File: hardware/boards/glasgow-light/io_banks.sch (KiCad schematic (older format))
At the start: 20 parts, among them J10 AUX, J4 Conn_01x02, U5 ICE40UP5K-SG48ITR

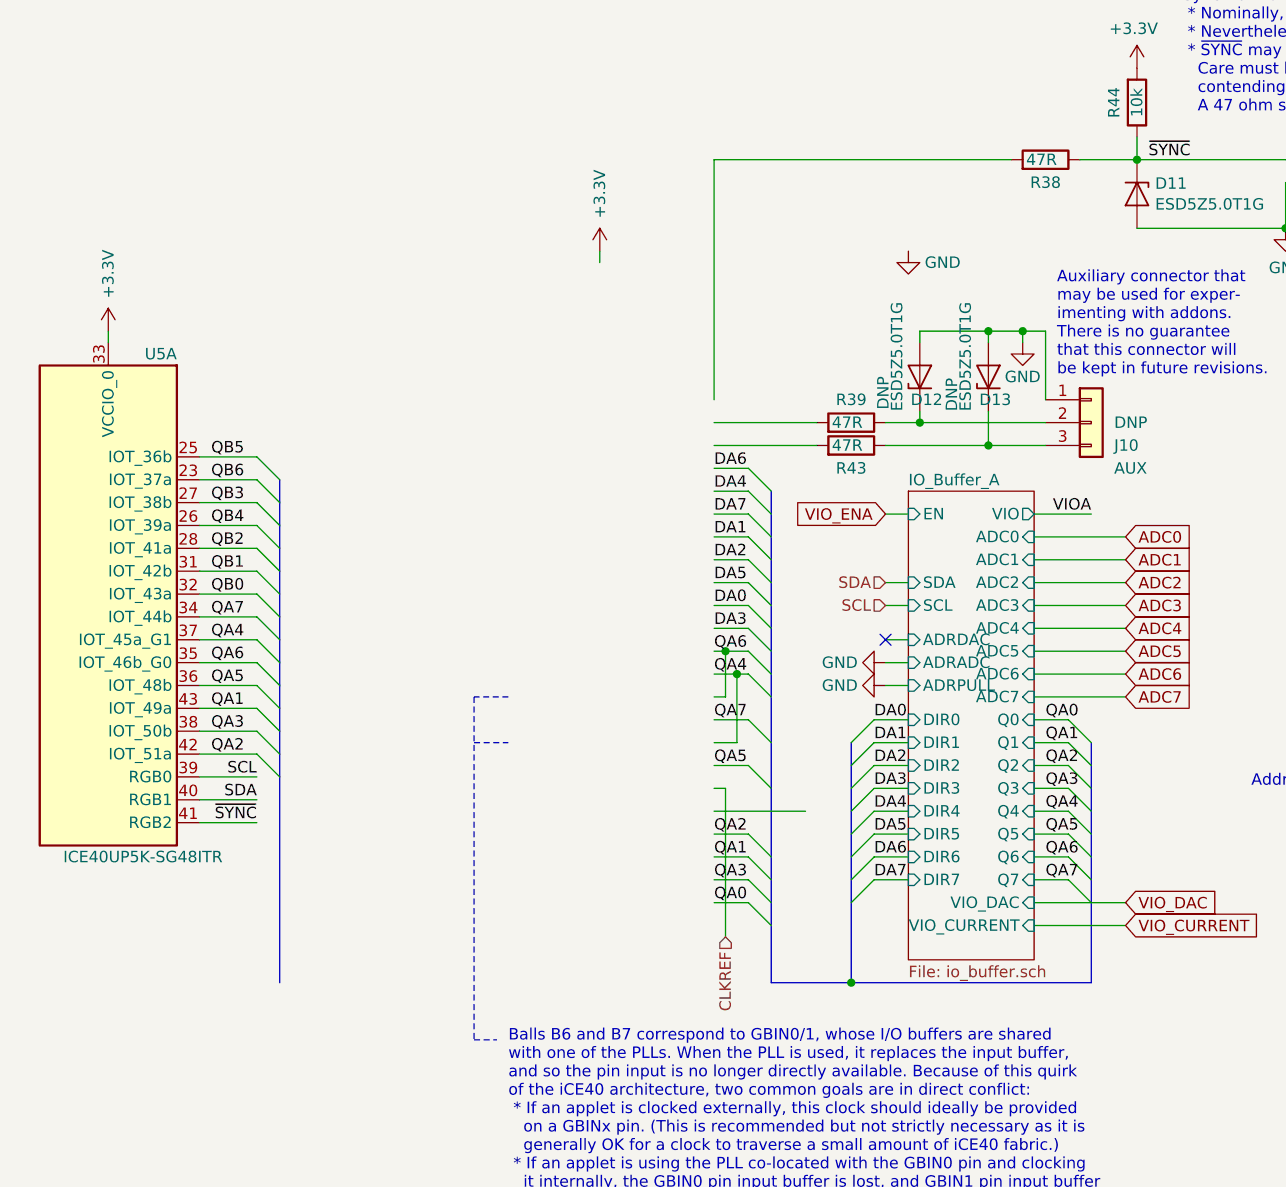
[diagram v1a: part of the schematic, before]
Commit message: start routing FPGA
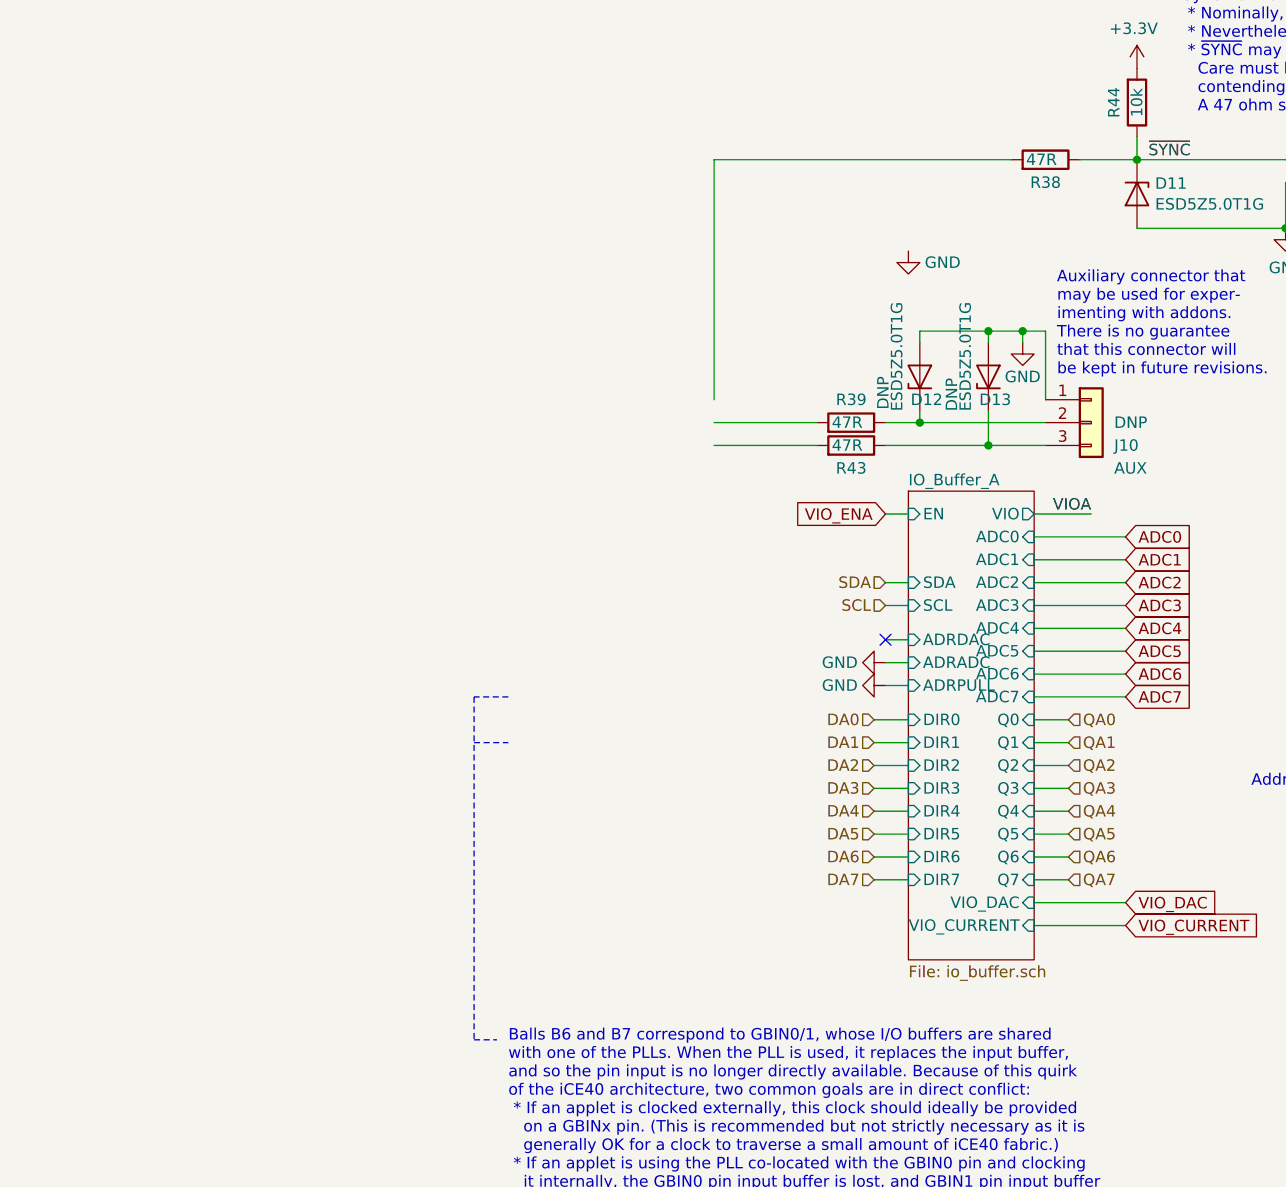
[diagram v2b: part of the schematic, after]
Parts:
- removed U5: ICE40UP5K-SG48ITR, Package_DFN_QFN:QFN-48-1EP_7x7mm_P0.5mm_EP5.15x5.15mm, symbol FPGA_Lattice:ICE40UP5K-SG48ITR
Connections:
- net labels removed: CLKREF, QB0, QB1, QB2, QB3, QB4, QB5, QB6
- wire segments 119 -> 75

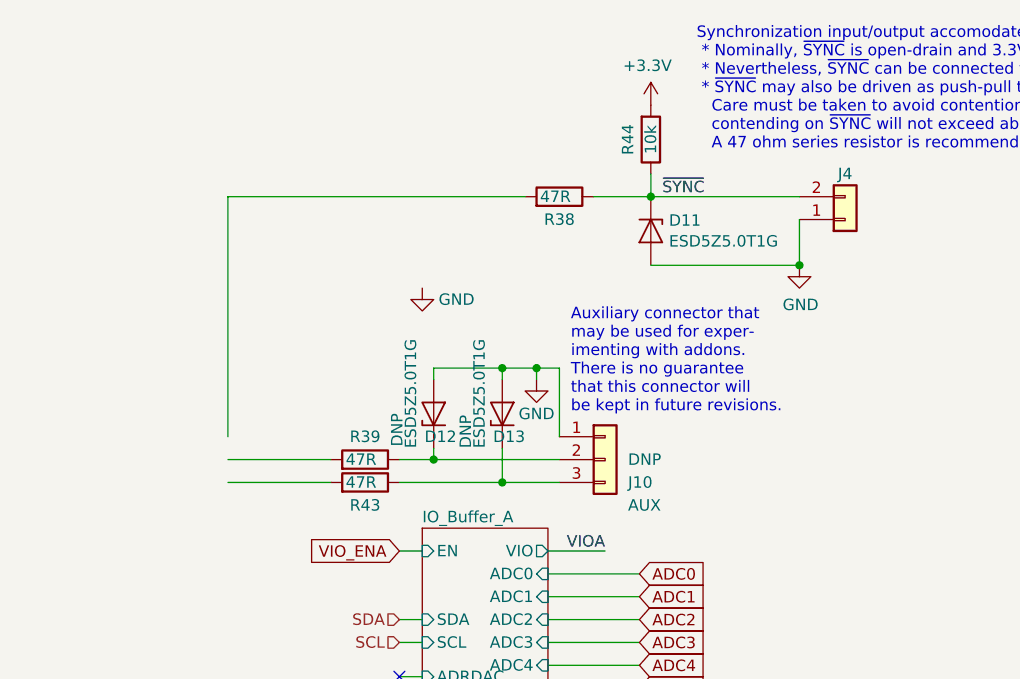
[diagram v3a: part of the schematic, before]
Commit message: replace SYNC and AUX connectors by test points
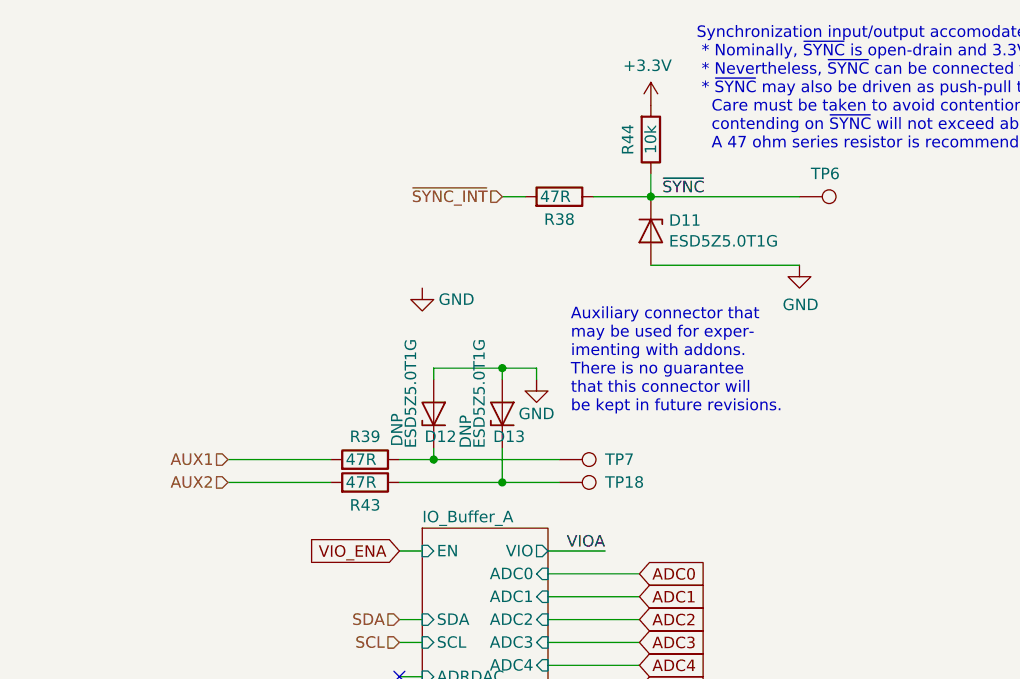
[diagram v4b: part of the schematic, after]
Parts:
- removed J10: AUX, Connector_PinHeader_2.54mm:PinHeader_1x03_P2.54mm_Vertical, symbol Connector_Generic:Conn_01x03
- removed J4: Conn_01x02, Glasgow:Molex_KK-254_1x02_P2.54mm_Horizontal, symbol Connector_Generic:Conn_01x02
- added TP18, TP6, TP7: SYNC, TestPoint:TestPoint_Pad_D1.0mm, symbol Connector:TestPoint
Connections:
- net labels added: AUX1, AUX2, ~SYNC_INT
- wire segments 75 -> 71
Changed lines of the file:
@@
 	2650 4250 2550 4250
-$Comp
-L Connector_Generic:Conn_01x03 J10
-U 1 1 5C072C23
-P 3450 3550
-F 0 "J10" H 3550 3450 50  0000 L CNN
-F 1 "AUX" H 3550 3350 50  0000 L CNN
-F 2 "Connector_PinHeader_2.54mm:PinHeader_1x03_P2.54mm_Vertical" H 3450 3550 50  0001 C CNN
-F 3 "~" H 3450 3550 50  0001 C CNN
-F 4 "conn-th-01in-3-1-hdr" H 3450 3550 50  0001 C CNN "1b2-bom-key"
-F 5 "DNP" H 3550 3550 50  0000 L CNN "DNP"
-	1    3450 3550
-	1    0    0    -1
-$EndComp
 $Comp
 L power:GND #PWR?
@@
 $EndComp
 $Comp
-L Connector_Generic:Conn_01x02 J?
-U 1 1 5C961091
-P 4500 2500
-AR Path="/5C961091" Ref="J?"  Part="1"
-AR Path="/5C7B59B0/5C961091" Ref="J4"  Part="1"
-F 0 "J4" H 4500 2300 50  0000 C CNN
-F 1 "Conn_01x02" H 4580 2401 50  0001 L CNN
-F 2 "Glasgow:Molex_KK-254_1x02_P2.54mm_Horizontal" H 4500 2500 50  0001 C CNN
-F 3 "https://www.mouser.hk/datasheet/2/418/NG_CD_640455_Y3-1255934.pdf" H 4500 2500 50  0001 C CNN
-F 4 "Molex" H -6100 -350 50  0001 C CNN "Mfg"
-F 5 "22-05-3021" H -6100 -350 50  0001 C CNN "MPN"
-F 6 "conn-th-01in-2-1-hdr-ra" H 4500 2500 50  0001 C CNN "1b2-bom-key"
-	1    4500 2500
-	1    0    0    1
-$EndComp
-$Comp
 L power:GND #PWR?
 U 1 1 5C961098
@@
 	1    0    0    -1
 $EndComp
-Wire Wire Line
-	1800 2400 1800 3450
 $Comp
 L Device:R R?
@@
 Connection ~ 3650 2400
 Wire Wire Line
-	4300 2500 4300 2700
-Connection ~ 4300 2700
-Wire Wire Line
 	3650 2400 4300 2400
 Wire Wire Line
@@
 $EndComp
 Wire Wire Line
-	3250 3150 3150 3150
-Wire Wire Line
 	3150 3150 3150 3200
 Wire Wire Line
-	3250 3150 3250 3450
-Wire Wire Line
 	3150 3150 3000 3150
 Wire Wire Line
 	3000 3150 3000 3200
-Connection ~ 3150 3150
 Wire Wire Line
 	3000 3150 2700 3150
@@
 $EndComp
 Wire Wire Line
-	1800 2400 3100 2400
+	3000 2400 3100 2400
 Wire Wire Line
 	2550 4700 2650 4700
@@
 Wire Wire Line
 	2650 5550 2500 5550
+Text HLabel 3000 2400 0    50   Input ~ 0
+~SYNC_INT
+$Comp
+L Connector:TestPoint TP?
+U 1 1 612A8BE6
+P 4300 2400
+AR Path="/612A8BE6" Ref="TP?"  Part="1"
+AR Path="/5C7B59B0/612A8BE6" Ref="TP6"  Part="1"
+F 0 "TP6" V 4200 2450 50  0000 L CNN
+F 1 "SYNC" V 4404 2474 50  0001 C CNN
+F 2 "TestPoint:TestPoint_Pad_D1.0mm" H 4500 2400 50  0001 C CNN
+F 3 "~" H 4500 2400 50  0001 C CNN
+	1    4300 2400
+	0    1    1    0
+$EndComp
+$Comp
+L Connector:TestPoint TP?
+U 1 1 6134742E
+P 3250 3550
+AR Path="/6134742E" Ref="TP?"  Part="1"
+AR Path="/5C7B59B0/6134742E" Ref="TP7"  Part="1"
+F 0 "TP7" V 3250 3750 50  0000 L CNN
+F 1 "SYNC" V 3354 3624 50  0001 C CNN
+F 2 "TestPoint:TestPoint_Pad_D1.0mm" H 3450 3550 50  0001 C CNN
+F 3 "~" H 3450 3550 50  0001 C CNN
+	1    3250 3550
+	0    1    1    0
+$EndComp
+$Comp
+L Connector:TestPoint TP?
+U 1 1 6134792A
+P 3250 3650
+AR Path="/6134792A" Ref="TP?"  Part="1"
+AR Path="/5C7B59B0/6134792A" Ref="TP18"  Part="1"
+F 0 "TP18" V 3250 3850 50  0000 L CNN
+F 1 "SYNC" V 3354 3724 50  0001 C CNN
+F 2 "TestPoint:TestPoint_Pad_D1.0mm" H 3450 3650 50  0001 C CNN
+F 3 "~" H 3450 3650 50  0001 C CNN
+	1    3250 3650
+	0    1    1    0
+$EndComp
+Text HLabel 1800 3550 0    50   Input ~ 0
+AUX1
+Text HLabel 1800 3650 0    50   Input ~ 0
+AUX2
 $EndSCHEMATC

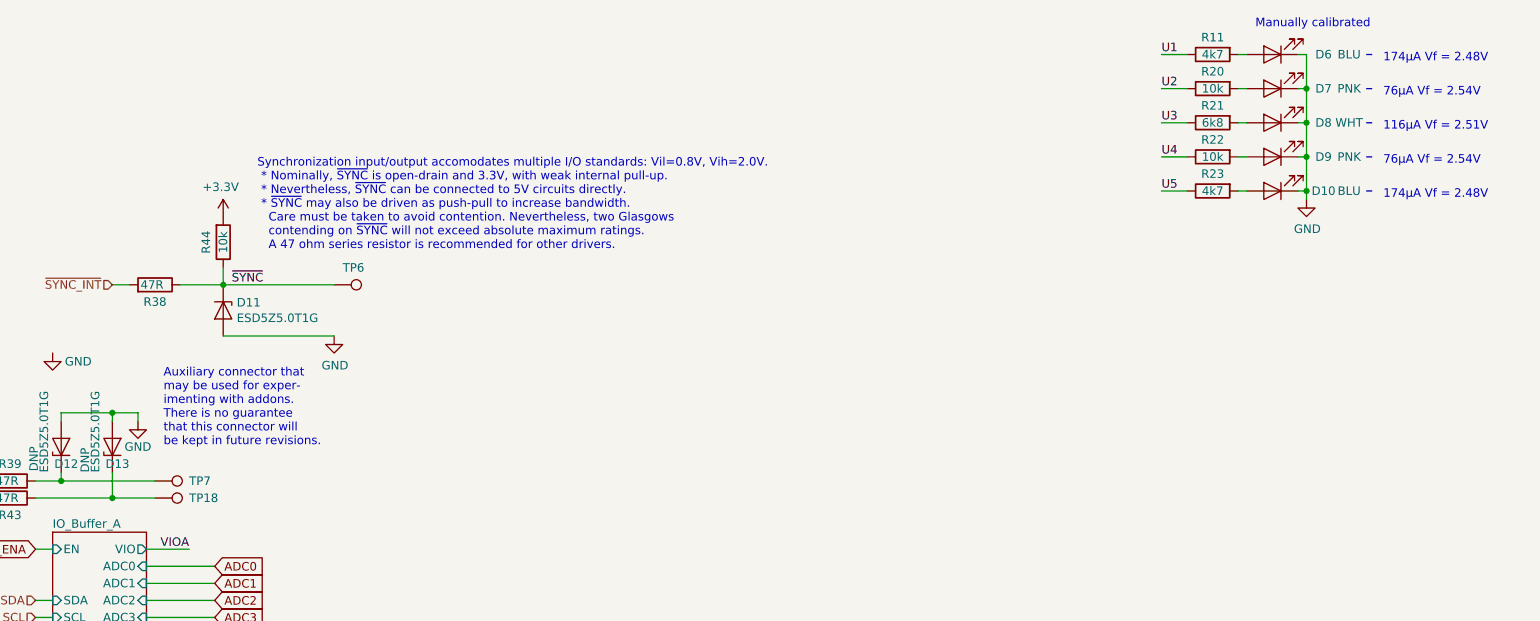
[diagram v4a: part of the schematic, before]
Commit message: most components are placed
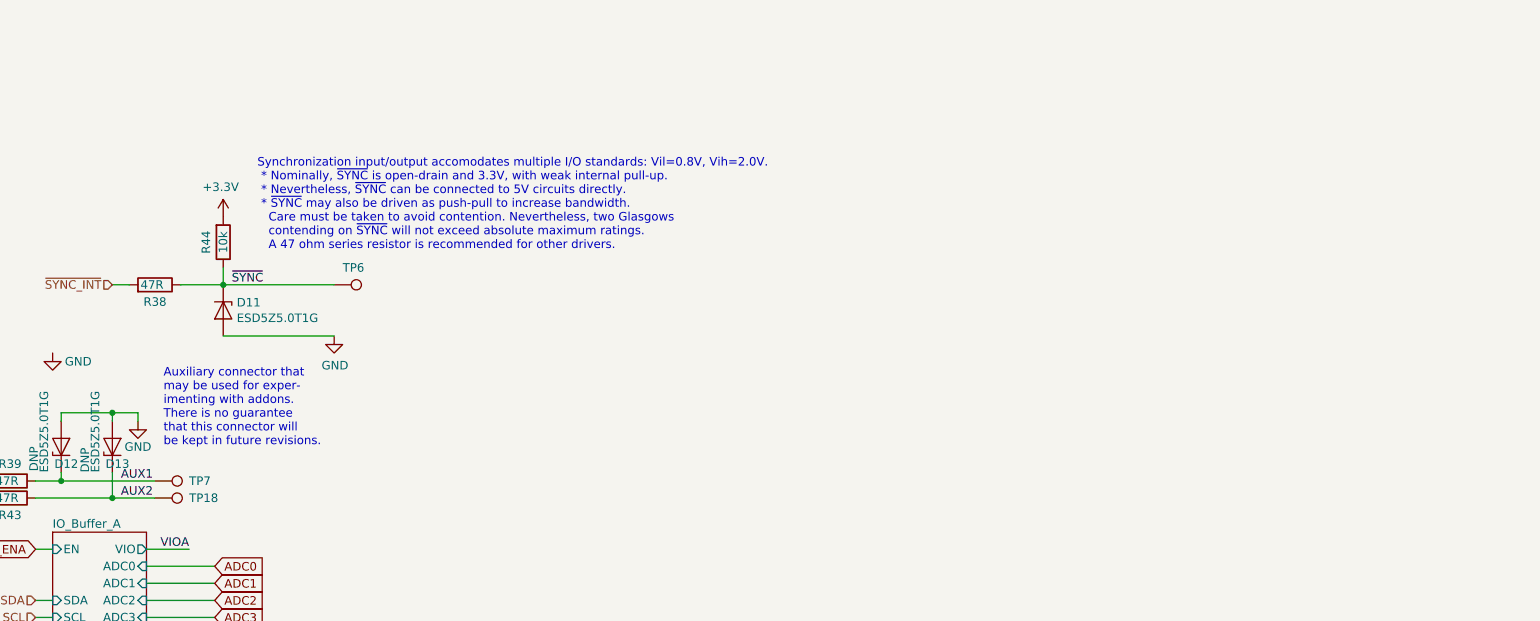
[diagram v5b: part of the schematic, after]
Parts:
- removed D10, D6: BLU, LED_SMD:LED_0603_1608Metric, symbol Device:LED
- removed D7, D9: PNK, LED_SMD:LED_0603_1608Metric, symbol Device:LED
- removed D8: WHT, LED_SMD:LED_0603_1608Metric, symbol Device:LED
- removed R11, R23: 4k7, Resistor_SMD:R_0402_1005Metric, symbol Device:R
- removed R20, R22: 10k, Resistor_SMD:R_0402_1005Metric, symbol Device:R
- removed R21: 6k8, Resistor_SMD:R_0402_1005Metric, symbol Device:R
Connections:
- net AUX1~: now reaches D12.1 (K), R39.1, TP7.1
- net AUX2~: now reaches D13.1 (K), R43.1, TP18.1
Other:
- note removed: "116µA Vf = 2.51V"
- note removed: "174µA Vf = 2.48V"
- note removed: "76µA Vf = 2.54V"
- note removed: "Manually calibrated"

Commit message: start optimizing silk
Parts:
- TP18: value SYNC -> AUX2
- TP7: value SYNC -> AUX1
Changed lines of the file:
@@
 AR Path="/5C7B59B0/6134742E" Ref="TP7"  Part="1"
 F 0 "TP7" V 3250 3750 50  0000 L CNN
-F 1 "SYNC" V 3354 3624 50  0001 C CNN
+F 1 "AUX1" V 3354 3624 50  0001 C CNN
 F 2 "TestPoint:TestPoint_Pad_D1.0mm" H 3450 3550 50  0001 C CNN
 F 3 "~" H 3450 3550 50  0001 C CNN
@@
 AR Path="/5C7B59B0/6134792A" Ref="TP18"  Part="1"
 F 0 "TP18" V 3250 3850 50  0000 L CNN
-F 1 "SYNC" V 3354 3724 50  0001 C CNN
+F 1 "AUX2" V 3354 3724 50  0001 C CNN
 F 2 "TestPoint:TestPoint_Pad_D1.0mm" H 3450 3650 50  0001 C CNN
 F 3 "~" H 3450 3650 50  0001 C CNN
